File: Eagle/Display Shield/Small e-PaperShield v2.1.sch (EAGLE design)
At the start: 139 parts, among them J2 3300060P1-ST-TF-003A, J3 2.54-8p-male-SMD, J4 2.54-8p-male-SMD, J5 2.54-6p-male-SMD, J6 2.54-6p-male-SMD, J7 2.54-2x3p-female-SMD, Q10 MOSFET-P-044021001, Q11 2N7002, Q2 2N7002, Q3 MOSFET-P-044021001, Q5 MOSFET-P-044021001, Q7 MOSFET-P-044021001, Q8 2N7002, Q9 2N7002, SW1 BUTTON-4P-REINFORCE'TS-1188E', U2 XC6206-3.3-1300260P1, U3 74VHC125PW, U4 74VHC125PW, U5 GT20L16P1Y, U6 DNP, U7 EPD 1.44/2.0/2.7 inch, U8 DNP, U9 S-8120CNB-DRB-TF-G//200021001

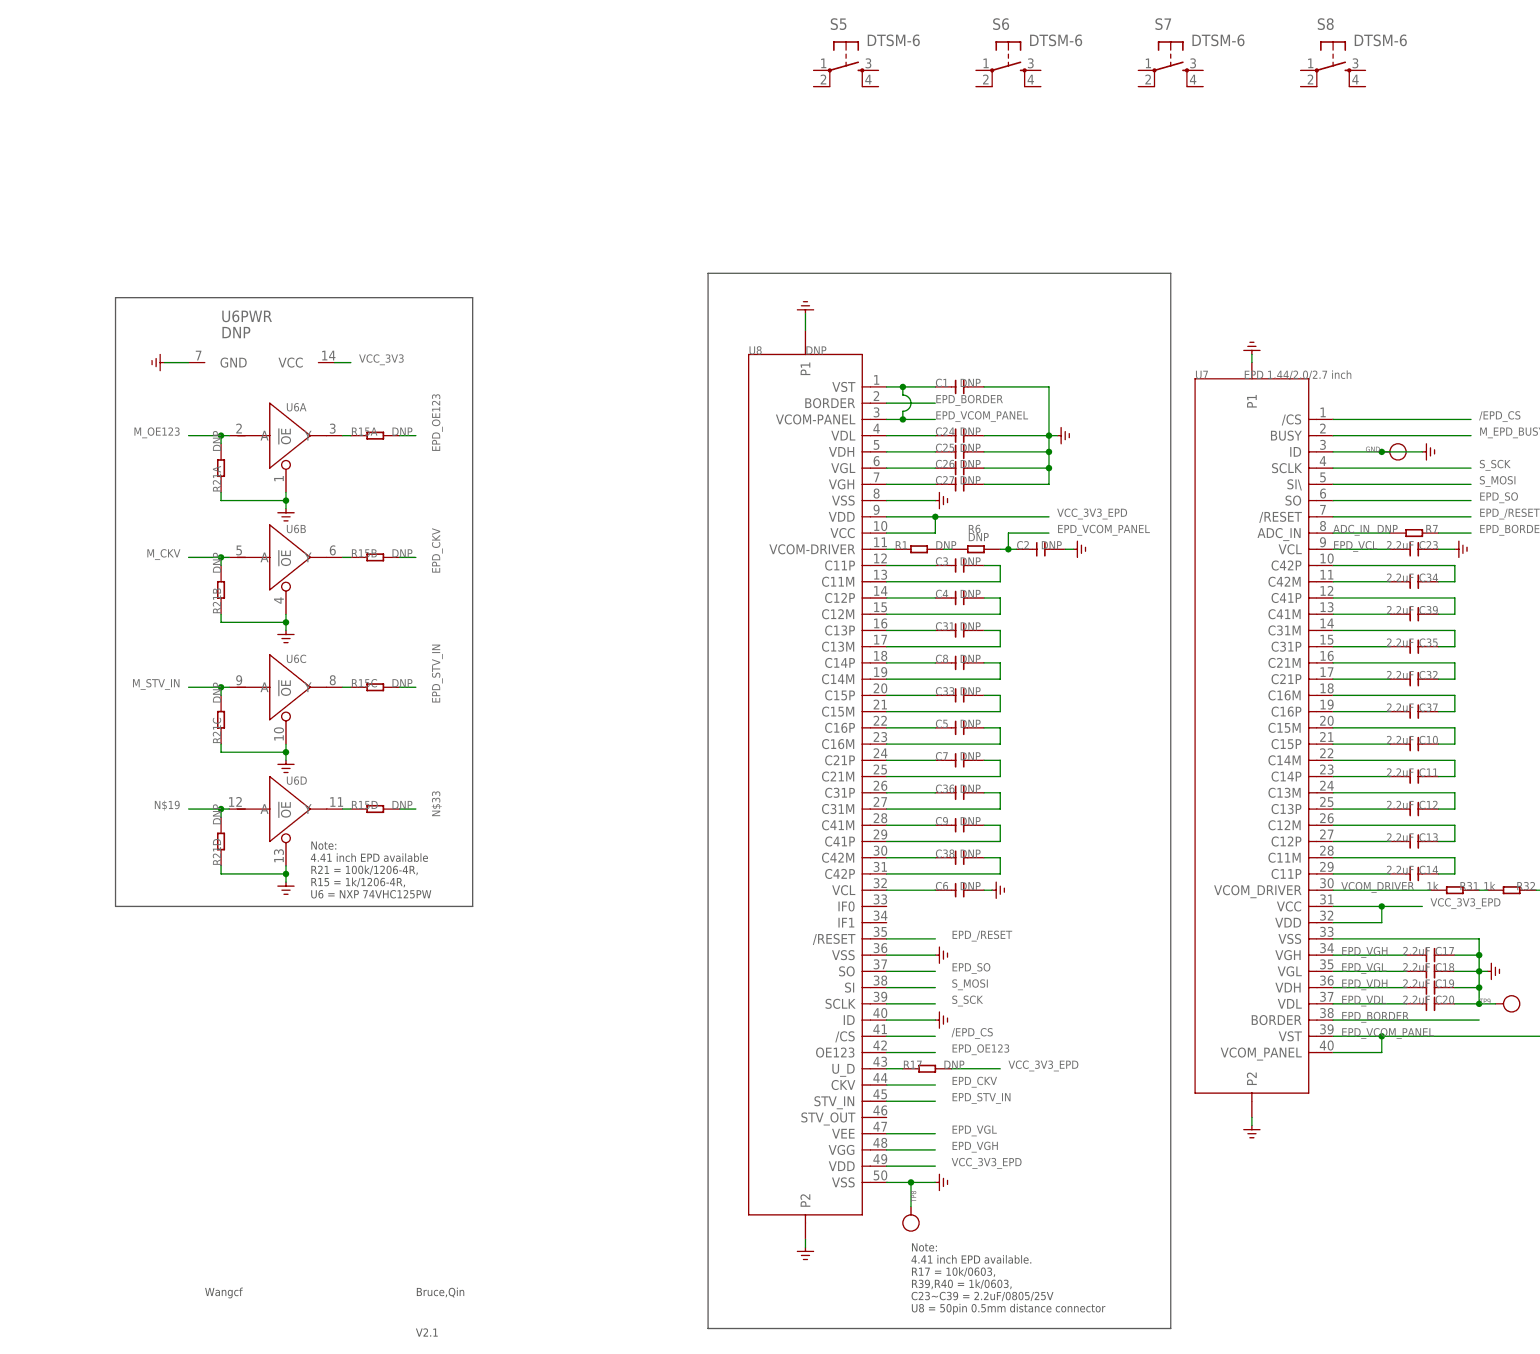
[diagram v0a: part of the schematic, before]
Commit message: removed all unnecessary components of display shield
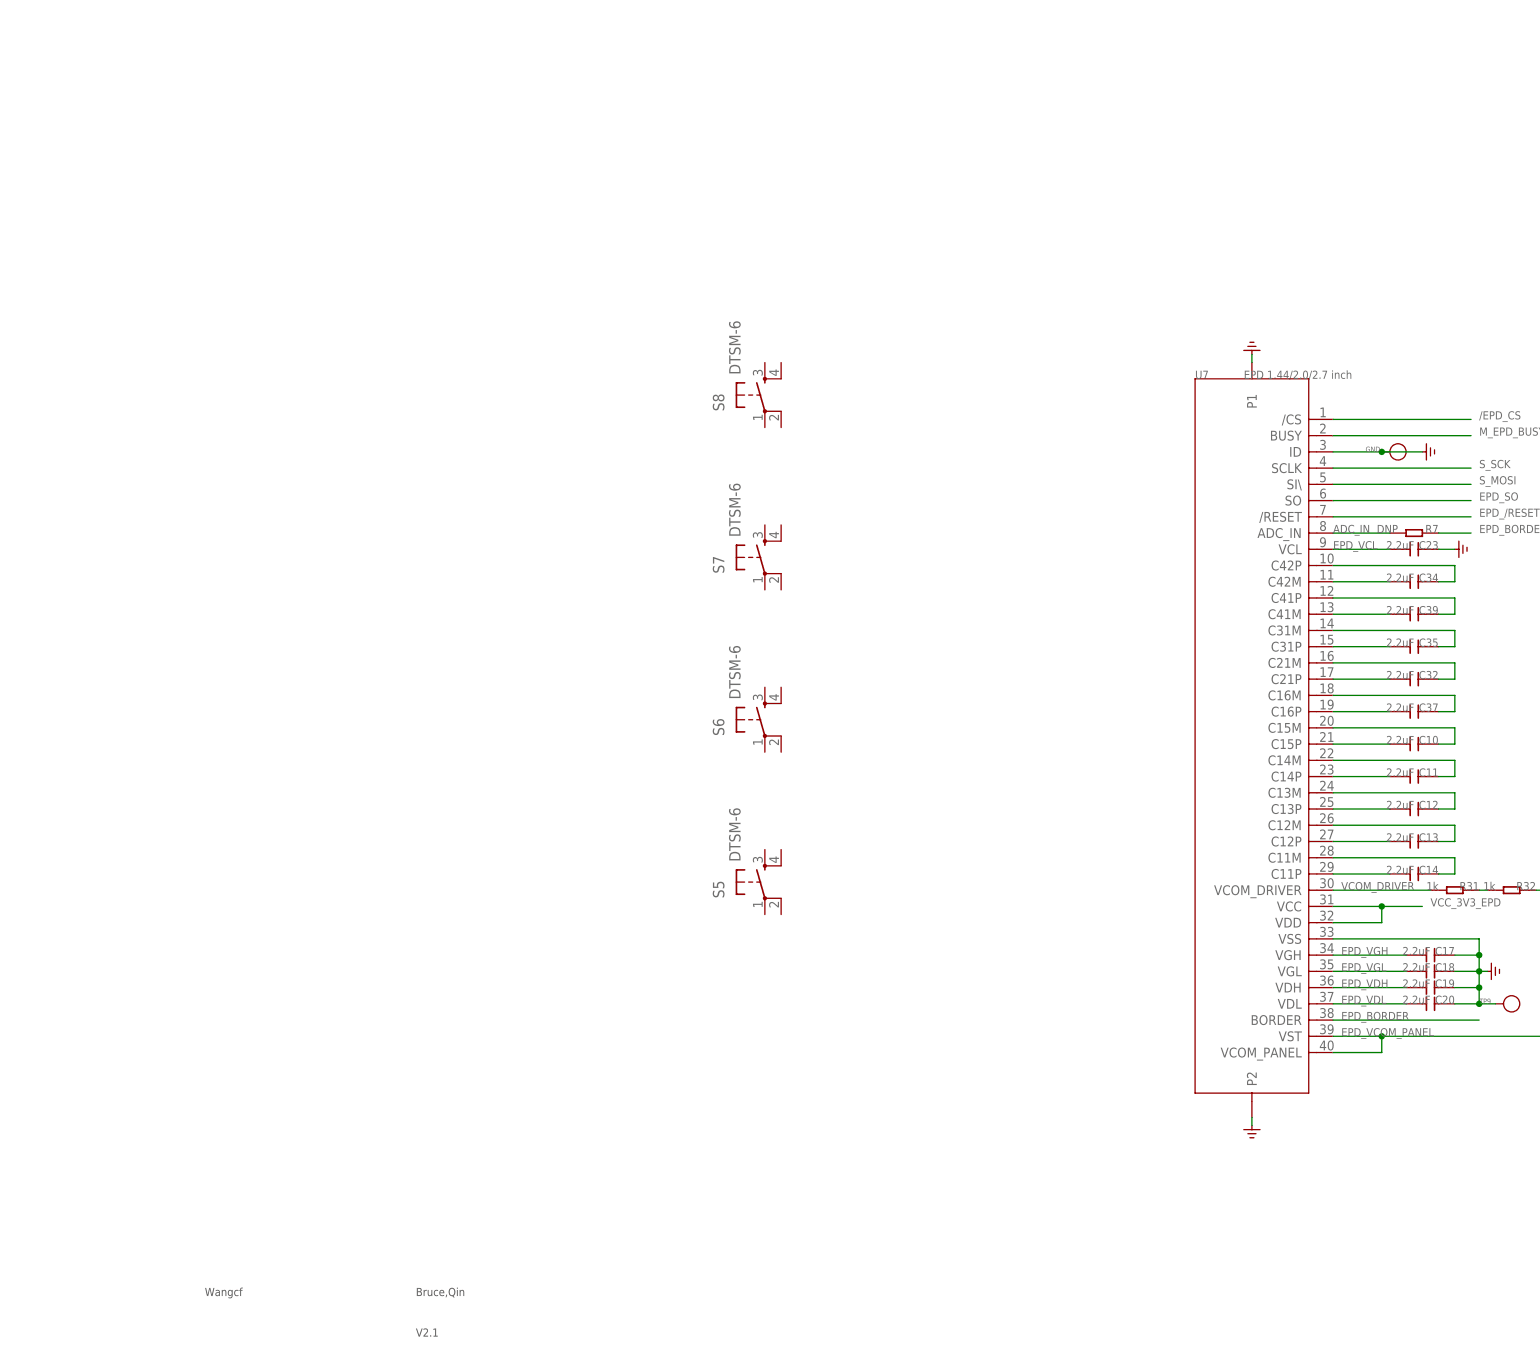
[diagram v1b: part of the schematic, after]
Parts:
- removed C1, C2, C24, C25, C26, C27, C3, C31, C33, C36, C38, C4, C5, C6, C7, C8, C9: DNP, Discrete:C-0805
- removed R1, R17, R6: DNP, Discrete:R-0603
- removed R15, R21: DNP, Discrete:R-4R-1206
- removed TP8: (no value), Discrete:PAD-TEST-POINT'3535'
- removed U6: DNP, IC:74VHC125PW
- removed U8: DNP, template:TFT-EPD-PANEL
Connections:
- removed net EPD_CKV: R15B.2, U8.CKV
- removed net EPD_OE123: R15A.2, U8.OE123
- removed net EPD_STV_IN: R15C.2, U8.STV_IN
- removed net N$15: C4.1, U8.C12P
- removed net N$19: R21D.2, U6D.A
- removed net N$23: R15A.1, U6A.Y
- removed net N$24: R15C.1, U6C.Y
- removed net N$25: R15D.1, U6D.Y
- removed net N$26: R15B.1, U6B.Y
- removed net N$30: R1.2, R6.1
- removed net N$33: R15D.2
- removed net N$39: C4.2, U8.C12M
- removed net N$40: C3.1, U8.C11P
- removed net N$41: C31.2, U8.C13M
- removed net N$42: C31.1, U8.C13P
- removed net N$43: C8.1, U8.C14P
- removed net N$44: C8.2, U8.C14M
- removed net N$45: C33.2, U8.C15M
- removed net N$46: C33.1, U8.C15P
- removed net N$47: C5.1, U8.C16P
- removed net N$48: C5.2, U8.C16M
- removed net N$49: C7.1, U8.C21P
- removed net N$50: C7.2, U8.C21M
- removed net N$51: C36.1, U8.C31P
- removed net N$52: C36.2, U8.C31M
- removed net N$53: C9.1, U8.C41M
- removed net N$54: C9.2, U8.C41P
- removed net N$55: C38.1, U8.C42M
- removed net N$56: C38.2, U8.C42P
- removed net N$57: C6.1, U8.VCL
- removed net N$58: R1.1, U8.VCOM-DRIVER
- removed net N$67: R17.1, U8.U_D
- removed net N$82: C3.2, U8.C11M
- net /EPD_CS: no longer U8./CS
- net EPD_/RESET: no longer U8./RESET
- net EPD_BORDER: no longer U8.BORDER
- net EPD_SO: no longer U8.SO
- net EPD_VCOM_PANEL: no longer C1.1, C2.1, R6.2, U8.VCOM-PANEL, U8.VST
- net EPD_VDH: no longer C25.1, U8.VDH
- net EPD_VDL: no longer C24.1, U8.VDL
- net EPD_VGH: no longer C27.1, U8.VGG, U8.VGH
- net EPD_VGL: no longer C26.1, U8.VEE, U8.VGL
- net GND: no longer C1.2, C2.2, C24.2, C25.2, C26.2, C27.2, C6.2, R21A.1, R21B.1, R21C.1, R21D.1, TP8.T, U6A.!OE, U6B.!OE, U6C.!OE, U6D.!OE, U6PWR.GND, U8.ID, U8.P1, U8.P2, U8.VSS, U8.VSS@1, U8.VSS@2
- net M_CKV: no longer R21B.2, U6B.A
- net M_OE123: no longer R21A.2, U6A.A
- net M_STV_IN: no longer R21C.2, U6C.A
- net S_MOSI: no longer U8.SI
- net S_SCK: no longer U8.SCLK
- net VCC_3V3: no longer U6PWR.VCC
- net VCC_3V3_EPD: no longer R17.2, U8.VCC, U8.VDD, U8.VDD@1
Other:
- note removed: "Note: 4.41 inch EPD available R21 = 100k/1206-4R, R15 = 1k/1206-4R, U6 = NXP 74VHC125PW"
- note removed: "Note: 4.41 inch EPD available. R17 = 10k/0603, R39,R40 = 1k/0603, C23~C39 = 2.2uF/0805/25V U8 = 50pin 0.5mm distance connector"
- moved on the sheet: S5, S6, S7, S8

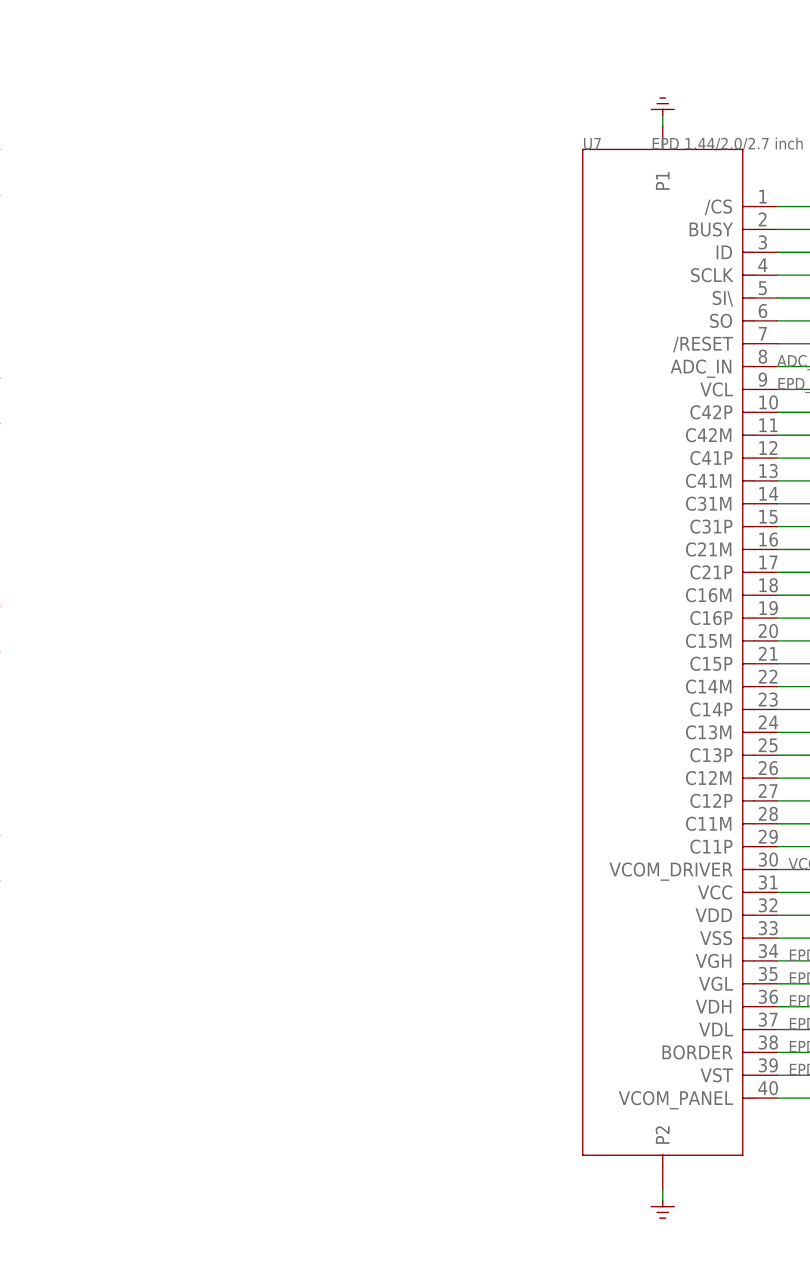
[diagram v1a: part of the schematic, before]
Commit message: re-placed components to board area, added 40pin connector. ready to go
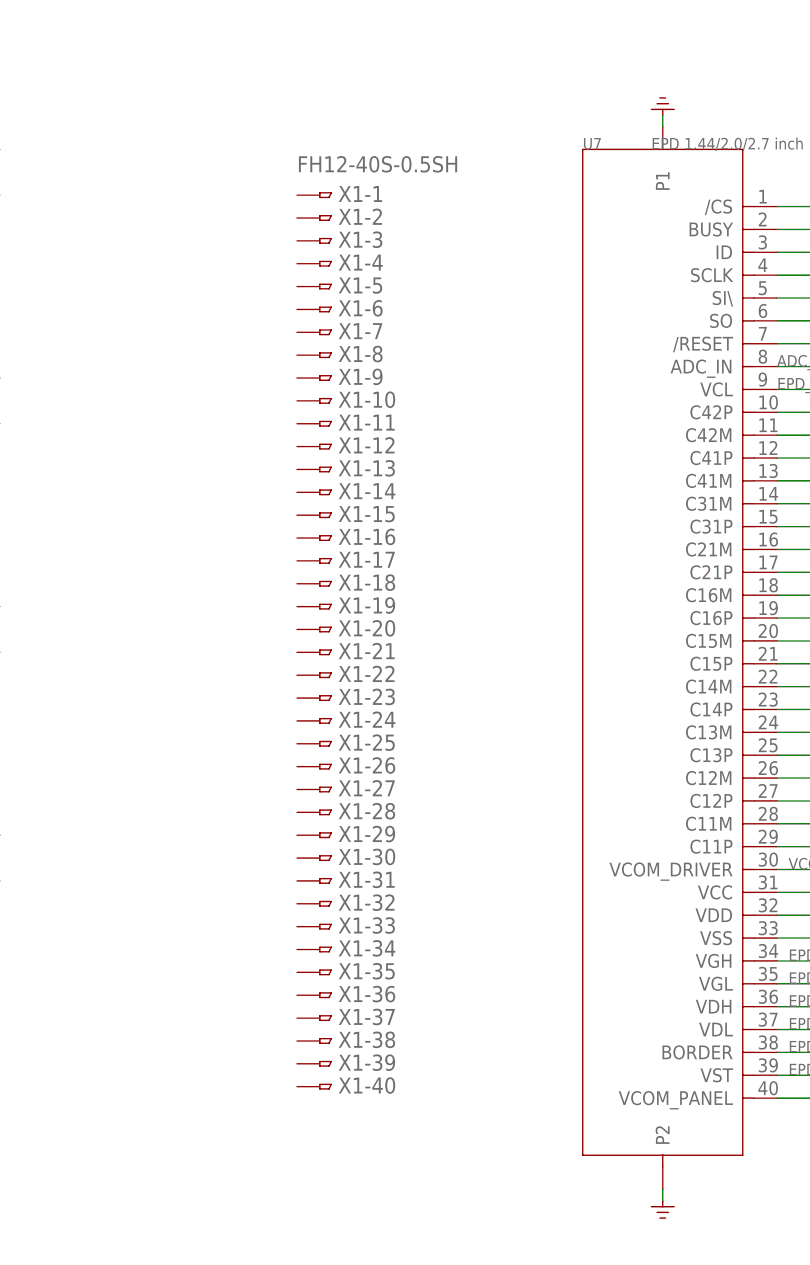
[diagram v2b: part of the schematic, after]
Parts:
- added X1: FH12-40S-0.5SH, con-hirose:FH12-40S-0.5SH
